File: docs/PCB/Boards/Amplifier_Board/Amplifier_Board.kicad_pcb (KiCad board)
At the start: 2 copper layers, 64.2 x 35.6 mm, 20 parts, among them J1 COM, Q1 AO3407A, SW1 SW_DIP_x04, U1 M24C32-WMN6TP, U2 SIP32431DR3-T1GE3

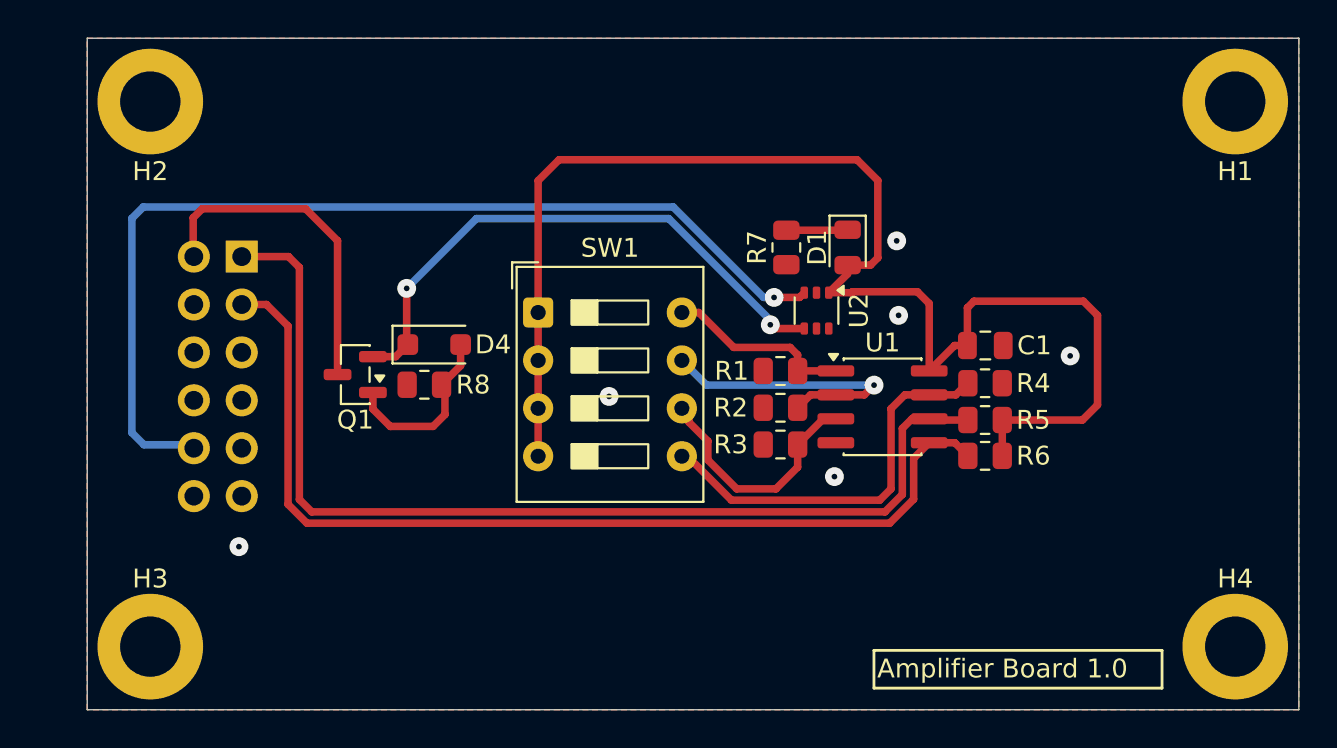
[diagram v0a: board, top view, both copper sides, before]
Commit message: Amplifier board added,base pico programs added.
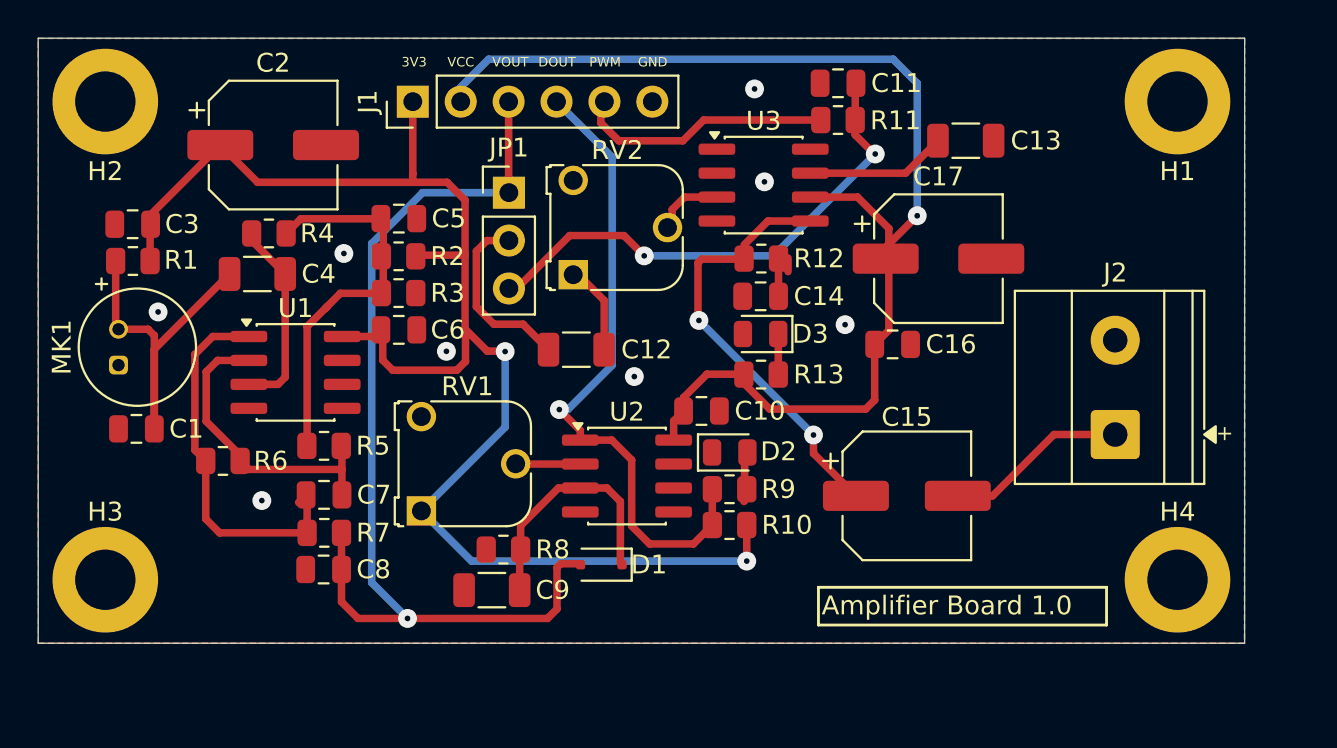
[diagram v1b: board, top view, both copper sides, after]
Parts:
- removed D4: BZT52C5V1-DIO, Diode_SMD:D_SOD-123F
- removed Q1: AO3407A, Package_TO_SOT_SMD:SOT-23
- removed SW1: SW_DIP_x04, Button_Switch_THT:SW_DIP_SPSTx04_Slide_9.78x12.34mm_W7.62mm_P2.54mm
- added C10: 100nF, Capacitor_SMD:C_0805_2012Metric, F.Cu at (138.7, 98.5)
- added C11: 10nF, Capacitor_SMD:C_0805_2012Metric, F.Cu at (145.9, 81.2)
- added C12: 4.7uF, Capacitor_SMD:C_1206_3216Metric, F.Cu at (132.0, 95.3)
- added C13: 10uF, Capacitor_SMD:C_1206_3216Metric, F.Cu at (152.7, 84.2)
- added C14: 100nF, Capacitor_SMD:C_0805_2012Metric, F.Cu at (141.8, 92.5)
- added C15: 220uF, Capacitor_SMD:CP_Elec_6.3x7.7, F.Cu at (149.6, 103.0)
- added C16: 100nF, Capacitor_SMD:C_0805_2012Metric, F.Cu at (148.8, 95.0)
- added C17: 100uF, Capacitor_SMD:CP_Elec_6.3x5.3, F.Cu at (151.2, 90.5)
- added C2: 100uF, Capacitor_SMD:CP_Elec_6.3x5.3, F.Cu at (116.0, 84.5)
- added C3: 100nF, Capacitor_SMD:C_0805_2012Metric, F.Cu at (108.5, 88.7)
- added C4: 1uF, Capacitor_SMD:C_1206_3216Metric, F.Cu at (115.1, 91.3)
- added C5: 100nF, Capacitor_SMD:C_0805_2012Metric, F.Cu at (122.6, 88.3)
- added C6: 100nF, Capacitor_SMD:C_0805_2012Metric, F.Cu at (122.6, 94.2)
- added C7: 100pF, Capacitor_SMD:C_0805_2012Metric, F.Cu at (118.6, 103.0)
- added C8: 100pF, Capacitor_SMD:C_0805_2012Metric, F.Cu at (118.6, 107.0)
- added C9: 4.7uF, Capacitor_SMD:C_1206_3216Metric, F.Cu at (127.5, 108.0)
- added D2: LED, LED_SMD:LED_0805_2012Metric, F.Cu at (140.2, 100.8)
- added D3: LED, LED_SMD:LED_0805_2012Metric, F.Cu at (141.8, 94.5)
- added J2: SPEAKER, TerminalBlock_Phoenix:TerminalBlock_Phoenix_MKDS-1,5-2_1x02_P5.00mm_Horizontal, F.Cu at (160.6, 99.8)
- added JP1: IN_SIGNAL, Connector_PinHeader_2.54mm:PinHeader_1x03_P2.54mm_Vertical, F.Cu at (128.4, 87.0)
- added MK1: Microphone, Sensor_Audio:POM-2244P-C3310-2-R, F.Cu at (107.8, 96.1)
- added R10: 10kR, Resistor_SMD:R_0805_2012Metric, F.Cu at (140.1, 104.6)
- added R11: 1kR, Resistor_SMD:R_0805_2012Metric, F.Cu at (145.9, 83.1)
- added R12: 10R, Resistor_SMD:R_0805_2012Metric, F.Cu at (141.8, 90.5)
- added R13: 1k2R, Resistor_SMD:R_0805_2012Metric, F.Cu at (141.8, 96.6)
- added R9: 1kR, Resistor_SMD:R_0805_2012Metric, F.Cu at (140.1, 102.7)
- added RV1: 10kR, Potentiometer_THT:Potentiometer_Runtron_RM-065_Vertical, F.Cu at (123.8, 103.8)
- added RV2: 10kR, Potentiometer_THT:Potentiometer_Runtron_RM-065_Vertical, F.Cu at (131.9, 91.3)
- added U3: LM386, Package_SO:SOIC-8_3.9x4.9mm_P1.27mm, F.Cu at (142.0, 86.6)
- D1: value LED -> BAT54W; footprint LED_SMD:LED_0805_2012Metric -> Diode_SMD:D_SOD-323F
- J1: value COM -> Conn_01x06_Pin; footprint Connector_PinHeader_2.54mm:PinHeader_2x06_P2.54mm_Vertical -> Connector_PinHeader_2.54mm:PinHeader_1x06_P2.54mm_Vertical; moved to F.Cu
- R1: value 47K -> 4k7R
- R2, R3: value 47K -> 100kR
- R4: value 47K -> 1MR
- R5: value 0 -> 2K2R
- R6: value 0 -> 47kR
- R7: value 1K -> 100R
- R8: value 100K -> 100kR
- U1: value M24C32-WMN6TP -> MCP6002-xSN
- U2: value SIP32431DR3-T1GE3 -> LM393; footprint Package_TO_SOT_SMD:SOT-363_SC-70-6 -> Package_SO:SOIC-8_3.9x4.9mm_P1.27mm
- moved C1 45.2 mm to (108.7, 99.5), turned to 180 degrees
- moved R6 40.4 mm to (113.3, 101.2)
- moved R4 38.8 mm to (115.7, 89.1)
- moved R5 35.1 mm to (118.7, 100.4), turned to 180 degrees
- moved R1 34.8 mm to (108.5, 90.6), turned to 180 degrees
- moved U1 31.2 mm to (117.1, 96.5)
- moved R7 28.8 mm to (118.7, 105.0), turned to 180 degrees
- moved R2 21.8 mm to (122.6, 90.3), turned to 180 degrees
- moved R3 21.8 mm to (122.6, 92.3)
- moved D1 21.3 mm to (133.3, 106.7), turned to 180 degrees
- moved U2 13.3 mm to (134.7, 102.0), turned to 0 degrees
- moved J1 12.2 mm to (123.4, 82.2), turned to 90 degrees
- moved R8 9.69 mm to (128.2, 105.9)
- moved H4 4.68 mm to (163.9, 107.5)
- moved H3 4.27 mm to (107.0, 107.5)
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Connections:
- C1 pad 1: 3V3_EEPROM -> Net-(MK1-+)
- D1 pad 2: 3V3_EEPROM -> VOUT_A
- J1 pad 1: I2C0_SCL -> 3V3
- J1 pad 2: 3V3_IN -> VCC
- J1 pad 3: I2C0_SDA -> VOUT_A
- J1 pad 4: unconnected-(J1-Pin_4-Pad4) -> DOUT
- J1 pad 5: unconnected-(J1-Pin_5-Pad5) -> Net-(J1-Pin_5)
- J1 pad 6: unconnected-(J1-Pin_6-Pad6) -> GND
- R1 pad 1: GND -> 3V3
- R1 pad 2: Net-(U1-E0) -> Net-(MK1-+)
- R2 pad 1: GND -> 3V3
- R2 pad 2: Net-(U1-E1) -> 1V65
- R3 pad 1: GND -> 1V65
- R3 pad 2: Net-(U1-E2) -> GND
- R4 pad 1: GND -> 1V65
- R4 pad 2: Net-(U1-~{WC}) -> VIN_AC
- R5 pad 1: I2C0_SCL -> Net-(U1A--)
- R5 pad 2: 3V3_EEPROM -> 1V65
- R6 pad 1: I2C0_SDA -> Net-(C7-Pad2)
- R6 pad 2: 3V3_EEPROM -> Net-(U1A--)
- R7 pad 1: GND -> VOUT_A
- R7 pad 2: Net-(D1-K) -> Net-(C7-Pad2)
- R8 pad 2: Net-(D4-A) -> Net-(D1-K)
- U1 pad 1: Net-(U1-E0) -> Net-(C7-Pad2)
- U1 pad 2: Net-(U1-E1) -> Net-(U1A--)
- U1 pad 3: Net-(U1-E2) -> VIN_AC
- U1 pad 5: I2C0_SDA -> unconnected-(U1B-+-Pad5)
- U1 pad 6: I2C0_SCL -> unconnected-(U1B---Pad6)
- U1 pad 7: Net-(U1-~{WC}) -> unconnected-(U1-Pad7)
- U1 pad 8: 3V3_EEPROM -> 3V3
- U2 pad 1: 3V3_EEPROM -> DOUT
- U2 pad 2: GND -> Net-(U2A--)
- U2 pad 3: ON -> Net-(D1-K)
- U2 pad 4: 3V3_OUT -> GND
- U2 pad 5: GND -> unconnected-(U2B-+-Pad5)
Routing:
- net 3V3: track 0.00 -> 78.8 mm, vias 0 -> 2
- net 3V3_EEPROM: track 74.6 -> 0.00 mm
- net VCC: track 0.00 -> 64.7 mm, vias 0 -> 1
- net I2C0_SCL: track 55.4 -> 0.00 mm
- net VOUT_A: track 0.00 -> 53.5 mm, vias 0 -> 1
- net ON: track 53.2 -> 0.00 mm, vias 1 -> 0
- net I2C0_SDA: track 52.2 -> 0.00 mm
- net DOUT: track 0.00 -> 34.7 mm, vias 0 -> 1
- net 3V3_OUT: track 30.5 -> 0.00 mm, vias 2 -> 0
- net PWM_OUT: track 0.00 -> 27.2 mm, vias 0 -> 2
- net Net-(C15-Pad1): track 0.00 -> 22.4 mm, vias 0 -> 2
- net 1V65: track 0.00 -> 20.7 mm
- net Net-(MK1-+): track 0.00 -> 20.5 mm
- net Net-(U1-~{WC}): track 20.3 -> 0.00 mm
- net Net-(C7-Pad2): track 0.00 -> 20.2 mm
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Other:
- board size 64.2 x 35.6 mm -> 64 x 32.1 mm
- board text added: "+"
- board text added: "3V3"
- board text added: "DOUT"
- board text added: "GND"
- board text added: "PWM"
- board text added: "VCC"
- board text added: "VOUT"

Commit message: Code review
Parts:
- added C18: 47nF, Capacitor_SMD:C_0805_2012Metric, F.Cu at (152.4, 83.1)
- added D4: 1N4148W, Diode_SMD:D_SOD-123, F.Cu at (122.3, 87.5)
- added D5: 1N4148W, Diode_SMD:D_SOD-123, F.Cu at (122.4, 85.1)
- added R14: 1kR, Resistor_SMD:R_0805_2012Metric, F.Cu at (131.9, 85.6)
- added R15: 1kR, Resistor_SMD:R_0805_2012Metric, F.Cu at (152.4, 81.2)
- J1: value Conn_01x06_Pin -> CON
- moved RV2 2.80 mm to (131.8, 94.1)
- moved C5 1.60 mm to (122.6, 90.0)
- moved R2 1.60 mm to (122.6, 92.0)
- moved R3 1.60 mm to (122.6, 93.9)
- moved C6 1.60 mm to (122.6, 95.8)
- moved C13 1.48 mm to (152.7, 85.7)
- moved C12 1.15 mm to (132.0, 96.5)
- moved C2 1.15 mm to (114.8, 84.5)
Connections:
- C11 pad 1: PWM_OUT -> Net-(C11-Pad1)
- J1 pad 3: VOUT_A -> Net-(D4-K)
- R11 pad 1: PWM_OUT -> Net-(C11-Pad1)
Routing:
- net Net-(D4-K): track 0.00 -> 15.4 mm, vias 0 -> 1
- net Net-(C11-Pad1): track 0.00 -> 6.72 mm
- net 3V3: track 78.8 -> 85.5 mm
- net PWM_OUT: track 27.2 -> 32.8 mm
- net Net-(U3-+): track 3.70 -> 6.58 mm
- net LM_IN: track 10.00 -> 11.1 mm
- net VOUT_A: track 53.5 -> 54.5 mm
- net Net-(C12-Pad2): track 4.58 -> 3.58 mm
- net Net-(U3-BYPASS): track 7.48 -> 6.89 mm
- net GND: track 0.07 -> 0.18 mm, vias 8 -> 7
